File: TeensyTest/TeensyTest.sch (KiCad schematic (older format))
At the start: 31 parts, among them J2 Conn_01x08_Female, J3 Conn_01x03_Female, P1 USB_C_Plug_USB2.0, SW1 SW_Push, SW2 SW_Push, U1 AP2114H, U2 MK20DX256VLH7, U3 MKL02Z32VFG4, Y1 Crystal_GND24

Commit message: Added BOM, added more pictures, added MPN's for some parts
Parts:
- P1: MFGR (none) -> Korean Hroparts Elec
- SW1, SW2: MFGR (none) -> Panasonic; MPN (none) -> EVQ-Q2B03W
- U2: MFGR (none) -> NXP; MPN (none) -> MK20DX256VLH7
- U3: MFGR (none) -> PJRC
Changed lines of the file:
@@
 F 2 "footprints:MK20DX256VLH7" H 12600 2140 60  0001 C CNN
 F 3 "" H 5300 1900 60  0000 C CNN
+F 4 "NXP" H 5300 1900 50  0001 C CNN "MFGR"
+F 5 "MK20DX256VLH7" H 5300 1900 50  0001 C CNN "MPN"
 	1    5300 1900
 	1    0    0    -1
@@
 F 1 "USB_C_Plug_USB2.0" H 2807 3126 50  0000 C CNN
 F 2 "USB-C-Power-tester:TYPE-C-31-M-12" H 2850 2350 50  0001 C CNN
-F 3 "" H 2850 2350 50  0001 C CNN
+F 3 "https://lcsc.com/product-detail/USB-Connectors_Korean-Hroparts-Elec-TYPE-C-31-M-12_C165948.html" H 2850 2350 50  0001 C CNN
 F 4 "TYPE-C-31-M-12" H 2700 2350 50  0001 C CNN "MPN"
+F 5 "Korean Hroparts Elec" H 2700 2350 50  0001 C CNN "MFGR"
 	1    2700 2350
 	1    0    0    -1
@@
 F 1 "MKL02Z32VFG4" H 2700 6650 50  0000 C CNN
 F 2 "Package_DFN_QFN:QFN-16-1EP_3x3mm_P0.5mm_EP1.8x1.8mm" H 2450 4125 50  0001 L TNN
-F 3 "http://www.nxp.com/docs/en/data-sheet/KL02P32M48SF0.pdf" H 2600 4550 50  0001 L BNN
+F 3 "https://www.pjrc.com/store/ic_mkl02.html" H 2600 4550 50  0001 L BNN
+F 4 "PJRC" H 2300 5350 50  0001 C CNN "MFGR"
 	1    2300 5350
 	0    1    1    0
@@
 F 2 "Button_Switch_SMD:SW_SPST_EVQQ2" H 2700 7750 50  0001 C CNN
 F 3 "" H 2700 7750 50  0001 C CNN
+F 4 "Panasonic" H 2700 7550 50  0001 C CNN "MFGR"
+F 5 "EVQ-Q2B03W" H 2700 7550 50  0001 C CNN "MPN"
 	1    2700 7550
 	0    1    1    0
@@
 F 2 "Button_Switch_SMD:SW_SPST_EVQQ2" H 15500 3200 50  0001 C CNN
 F 3 "" H 15500 3200 50  0001 C CNN
+F 4 "Panasonic" H 15500 3000 50  0001 C CNN "MFGR"
+F 5 "EVQ-Q2B03W" H 15500 3000 50  0001 C CNN "MPN"
 	1    15500 3000
 	1    0    0    -1

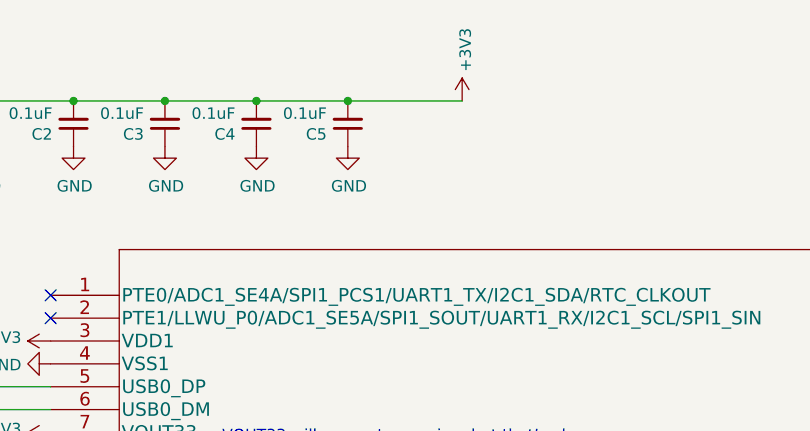
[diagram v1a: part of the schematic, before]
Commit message: Added extra 100nF cap for MKL02
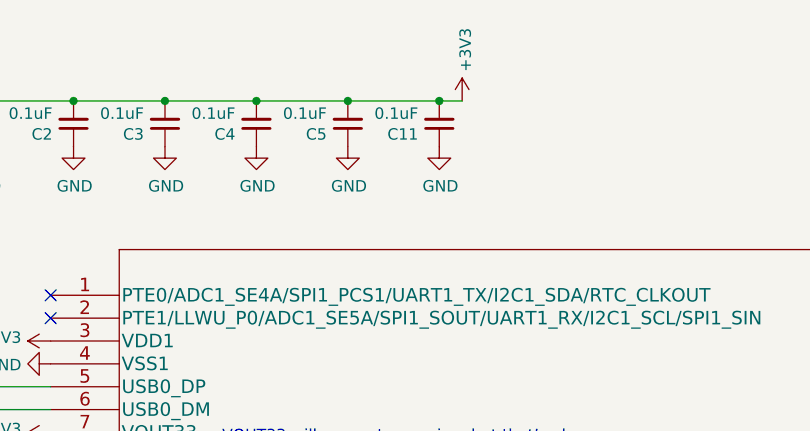
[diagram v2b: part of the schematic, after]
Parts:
- added C11: 0.1uF, Capacitor_SMD:C_0603_1608Metric, symbol Device:C_Small
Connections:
- net +3V3: now also C11.2
- net GND: now also C11.1
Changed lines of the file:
@@
 	4250 2250 4250 2400
 Wire Wire Line
-	6600 1050 7100 1050
+	6600 1050 7000 1050
 $Comp
 L power:+3V3 #PWR0125
@@
 Text Notes 6050 2550 0    50   ~ 0
 VOUT33 will generate warning, but that’s ok
+$Comp
+L Device:C_Small C11
+U 1 1 5F62A840
+P 7000 1150
+F 0 "C11" H 7092 1196 50  0000 L CNN
+F 1 "0.1uF" H 7092 1105 50  0000 L CNN
+F 2 "Capacitor_SMD:C_0603_1608Metric" H 7000 1150 50  0001 C CNN
+F 3 "~" H 7000 1150 50  0001 C CNN
+	1    7000 1150
+	-1   0    0    1
+$EndComp
+$Comp
+L power:GND #PWR0134
+U 1 1 5F62A84A
+P 7000 1250
+F 0 "#PWR0134" H 7000 1000 50  0001 C CNN
+F 1 "GND" H 7005 1077 50  0000 C CNN
+F 2 "" H 7000 1250 50  0001 C CNN
+F 3 "" H 7000 1250 50  0001 C CNN
+	1    7000 1250
+	1    0    0    -1
+$EndComp
+Connection ~ 7000 1050
+Wire Wire Line
+	7000 1050 7100 1050
 $EndSCHEMATC

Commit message: added Teensy3.2 schematic as reference, added CLK pin for SPI comms
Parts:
- J3: value Conn_01x03_Female -> Conn_01x04_Female; footprint Connector_PinHeader_2.54mm:PinHeader_1x03_P2.54mm_Vertical -> Connector_PinHeader_2.54mm:PinHeader_1x04_P2.54mm_Vertical; symbol Connector:Conn_01x03_Female -> Connector:Conn_01x04_Female
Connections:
- net D10: now also J3.4 (Pin_4); no longer J3.3 (Pin_3)
- net D13: now reaches U2.50 (PTC5/LLWU_P9/SPI0_SCK/LPTMR0_ALT2/I2S0_RXD0/FB_AD10/CMP0_OUT)
- net D13: now also J3.3 (Pin_3)
- no-connect marks 37 -> 36
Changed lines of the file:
@@
 D25
 $Comp
-L Connector:Conn_01x03_Female J3
+L Connector:Conn_01x04_Female J3
 U 1 1 5ED4B5DF
 P 15950 3300
 F 0 "J3" H 15978 3326 50  0000 L CNN
-F 1 "Conn_01x03_Female" H 15978 3235 50  0000 L CNN
-F 2 "Connector_PinHeader_2.54mm:PinHeader_1x03_P2.54mm_Vertical" H 15950 3300 50  0001 C CNN
+F 1 "Conn_01x04_Female" H 15978 3235 50  0000 L CNN
+F 2 "Connector_PinHeader_2.54mm:PinHeader_1x04_P2.54mm_Vertical" H 15950 3300 50  0001 C CNN
 F 3 "~" H 15950 3300 50  0001 C CNN
 	1    15950 3300
 	1    0    0    -1
 $EndComp
-Wire Wire Line
-	15750 3400 14450 3400
 Wire Wire Line
 	14450 3200 15400 3200
@@
 NoConn ~ 14450 3800
 NoConn ~ 14450 3700
-NoConn ~ 14450 3300
 NoConn ~ 14450 2900
 NoConn ~ 14450 2800
@@
 Wire Wire Line
 	7000 1050 7100 1050
+Wire Wire Line
+	15050 3400 15050 3500
+Wire Wire Line
+	15050 3500 15750 3500
+Wire Wire Line
+	14450 3400 15050 3400
+Wire Wire Line
+	14450 3300 15200 3300
+Wire Wire Line
+	15200 3300 15200 3400
+Wire Wire Line
+	15200 3400 15750 3400
+Text Label 14600 3300 0    50   ~ 0
+D13
 $EndSCHEMATC
